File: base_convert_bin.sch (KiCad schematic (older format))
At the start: 36 parts, among them Q18 Q_PNP_BEC, Q19 Q_PNP_BEC, Q20 Q_PNP_BEC, Q21 Q_PNP_BEC, Q22 Q_NPN_BEC, Q23 Q_NPN_BEC, Q24 Q_NPN_BEC, Q25 Q_NPN_BEC

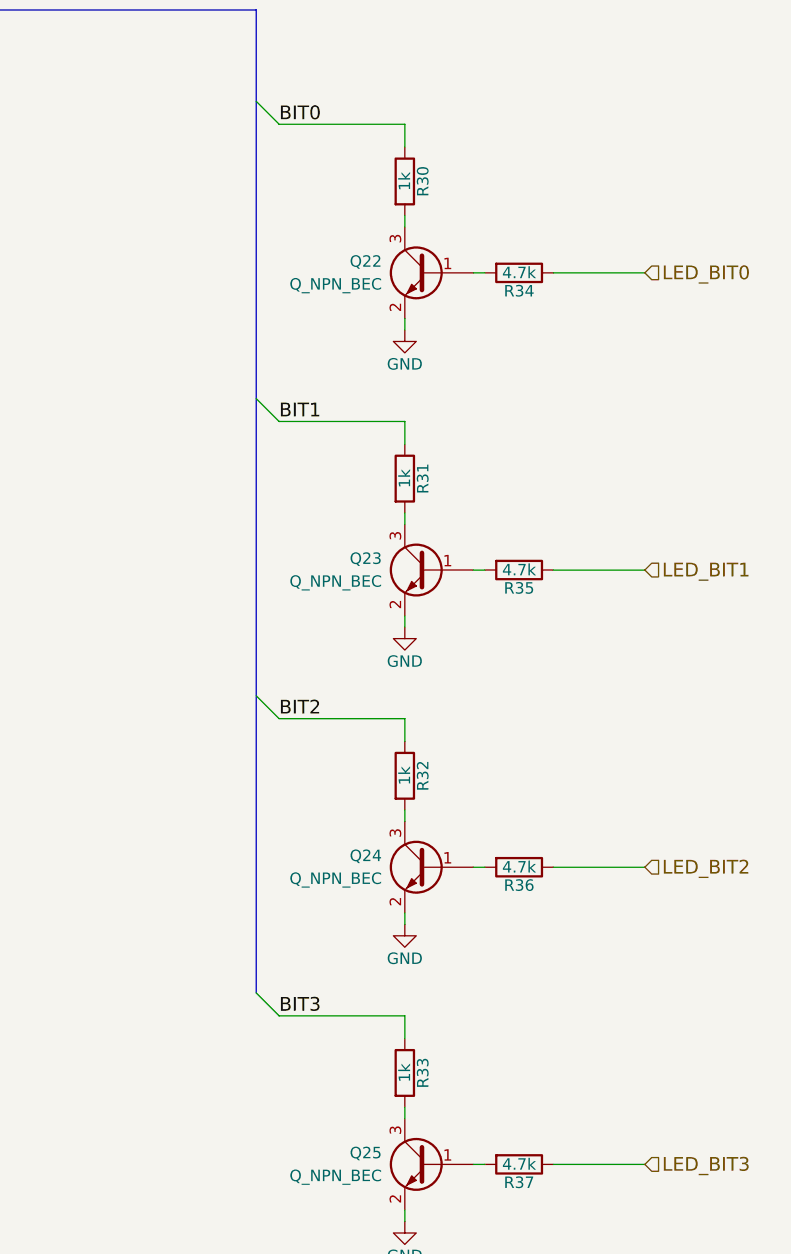
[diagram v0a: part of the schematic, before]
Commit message: change led current limit resistor value
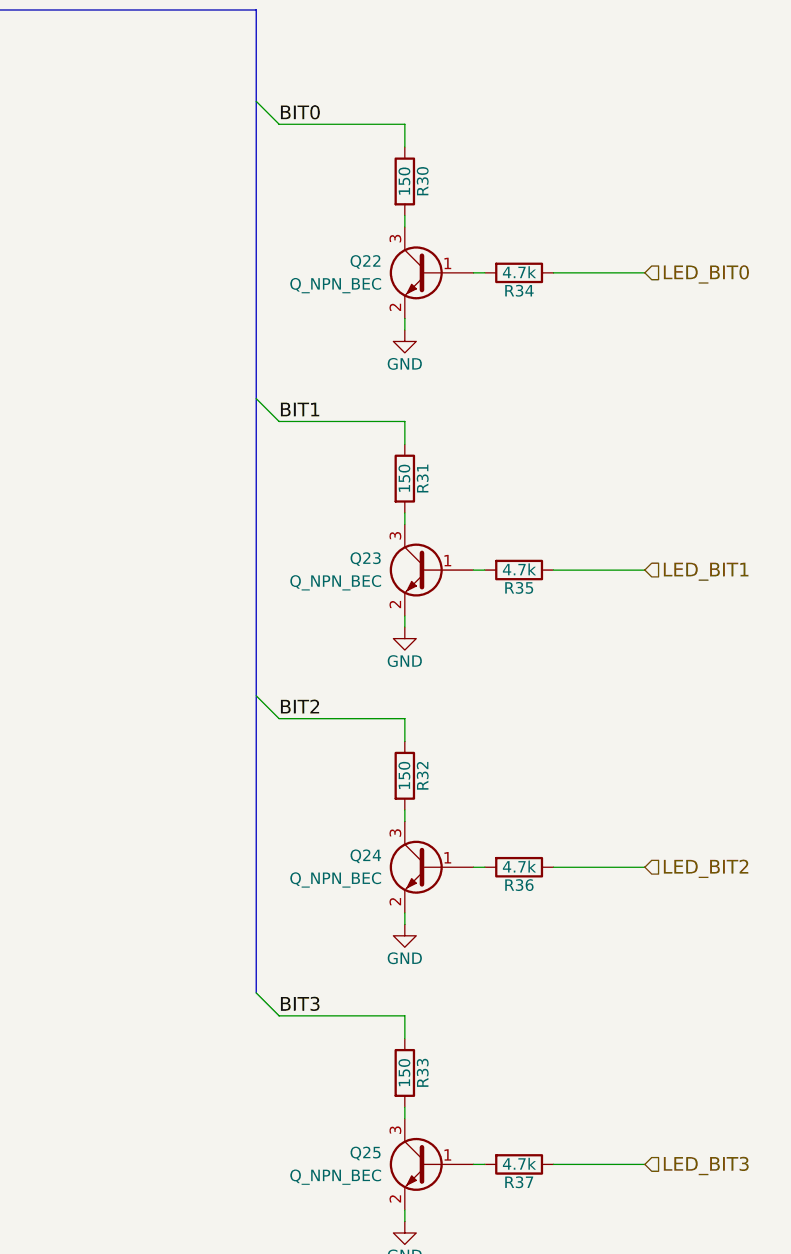
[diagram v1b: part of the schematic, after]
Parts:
- R30, R31, R32, R33: value 1k -> 150; Description (none) -> NONE; Manufacture (none) -> NONE; Mfg Part Number (none) -> NONE; Package (none) -> NONE
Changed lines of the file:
@@
 P 8250 1750
 F 0 "R30" V 8330 1750 50  0000 C CNN
-F 1 "1k" V 8250 1750 50  0000 C CNN
+F 1 "150" V 8250 1750 50  0000 C CNN
 F 2 "Resistors_SMD:R_0603" V 8180 1750 50  0001 C CNN
 F 3 "" H 8250 1750 50  0001 C CNN
+F 4 "NONE" H 8250 1750 60  0001 C CNN "Manufacture"
+F 5 "NONE" H 8250 1750 60  0001 C CNN "Mfg Part Number"
+F 6 "NONE" H 8250 1750 60  0001 C CNN "Package"
+F 7 "NONE" H 8250 1750 60  0001 C CNN "Description"
 	1    8250 1750
 	1    0    0    -1
@@
 P 8250 3050
 F 0 "R31" V 8330 3050 50  0000 C CNN
-F 1 "1k" V 8250 3050 50  0000 C CNN
+F 1 "150" V 8250 3050 50  0000 C CNN
 F 2 "Resistors_SMD:R_0603" V 8180 3050 50  0001 C CNN
 F 3 "" H 8250 3050 50  0001 C CNN
+F 4 "NONE" H 8250 3050 60  0001 C CNN "Manufacture"
+F 5 "NONE" H 8250 3050 60  0001 C CNN "Mfg Part Number"
+F 6 "NONE" H 8250 3050 60  0001 C CNN "Package"
+F 7 "NONE" H 8250 3050 60  0001 C CNN "Description"
 	1    8250 3050
 	1    0    0    -1
@@
 P 8250 4350
 F 0 "R32" V 8330 4350 50  0000 C CNN
-F 1 "1k" V 8250 4350 50  0000 C CNN
+F 1 "150" V 8250 4350 50  0000 C CNN
 F 2 "Resistors_SMD:R_0603" V 8180 4350 50  0001 C CNN
 F 3 "" H 8250 4350 50  0001 C CNN
+F 4 "NONE" H 8250 4350 60  0001 C CNN "Manufacture"
+F 5 "NONE" H 8250 4350 60  0001 C CNN "Mfg Part Number"
+F 6 "NONE" H 8250 4350 60  0001 C CNN "Package"
+F 7 "NONE" H 8250 4350 60  0001 C CNN "Description"
 	1    8250 4350
 	1    0    0    -1
@@
 P 8250 5650
 F 0 "R33" V 8330 5650 50  0000 C CNN
-F 1 "1k" V 8250 5650 50  0000 C CNN
+F 1 "150" V 8250 5650 50  0000 C CNN
 F 2 "Resistors_SMD:R_0603" V 8180 5650 50  0001 C CNN
 F 3 "" H 8250 5650 50  0001 C CNN
+F 4 "NONE" H 8250 5650 60  0001 C CNN "Manufacture"
+F 5 "NONE" H 8250 5650 60  0001 C CNN "Mfg Part Number"
+F 6 "NONE" H 8250 5650 60  0001 C CNN "Package"
+F 7 "NONE" H 8250 5650 60  0001 C CNN "Description"
 	1    8250 5650
 	1    0    0    -1

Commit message: update switch fields
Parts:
- R30, R31, R32, R33: Description NONE -> (none); Manufacture NONE -> (none); Mfg Part Number NONE -> (none); Package NONE -> (none)
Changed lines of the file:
@@
 F 2 "Resistors_SMD:R_0603" V 8180 1750 50  0001 C CNN
 F 3 "" H 8250 1750 50  0001 C CNN
-F 4 "NONE" H 8250 1750 60  0001 C CNN "Manufacture"
-F 5 "NONE" H 8250 1750 60  0001 C CNN "Mfg Part Number"
-F 6 "NONE" H 8250 1750 60  0001 C CNN "Package"
-F 7 "NONE" H 8250 1750 60  0001 C CNN "Description"
 	1    8250 1750
 	1    0    0    -1
@@
 $EndComp
 $Comp
-L VCC #PWR30
+L VCC #PWR29
 U 1 1 5AEDDAFD
 P 4300 750
-F 0 "#PWR30" H 4300 600 50  0001 C CNN
+F 0 "#PWR29" H 4300 600 50  0001 C CNN
 F 1 "VCC" H 4300 900 50  0000 C CNN
 F 2 "" H 4300 750 50  0001 C CNN
@@
 $EndComp
 $Comp
-L GND #PWR34
+L GND #PWR33
 U 1 1 5AEE40C6
 P 8250 2400
-F 0 "#PWR34" H 8250 2150 50  0001 C CNN
+F 0 "#PWR33" H 8250 2150 50  0001 C CNN
 F 1 "GND" H 8250 2250 50  0000 C CNN
 F 2 "" H 8250 2400 50  0001 C CNN
@@
 F 2 "Resistors_SMD:R_0603" V 8180 3050 50  0001 C CNN
 F 3 "" H 8250 3050 50  0001 C CNN
-F 4 "NONE" H 8250 3050 60  0001 C CNN "Manufacture"
-F 5 "NONE" H 8250 3050 60  0001 C CNN "Mfg Part Number"
-F 6 "NONE" H 8250 3050 60  0001 C CNN "Package"
-F 7 "NONE" H 8250 3050 60  0001 C CNN "Description"
 	1    8250 3050
 	1    0    0    -1
@@
 $EndComp
 $Comp
-L GND #PWR35
+L GND #PWR34
 U 1 1 5AEEC0D0
 P 8250 3700
-F 0 "#PWR35" H 8250 3450 50  0001 C CNN
+F 0 "#PWR34" H 8250 3450 50  0001 C CNN
 F 1 "GND" H 8250 3550 50  0000 C CNN
 F 2 "" H 8250 3700 50  0001 C CNN
@@
 F 2 "Resistors_SMD:R_0603" V 8180 4350 50  0001 C CNN
 F 3 "" H 8250 4350 50  0001 C CNN
-F 4 "NONE" H 8250 4350 60  0001 C CNN "Manufacture"
-F 5 "NONE" H 8250 4350 60  0001 C CNN "Mfg Part Number"
-F 6 "NONE" H 8250 4350 60  0001 C CNN "Package"
-F 7 "NONE" H 8250 4350 60  0001 C CNN "Description"
 	1    8250 4350
 	1    0    0    -1
@@
 $EndComp
 $Comp
-L GND #PWR36
+L GND #PWR35
 U 1 1 5AEEC4A2
 P 8250 5000
-F 0 "#PWR36" H 8250 4750 50  0001 C CNN
+F 0 "#PWR35" H 8250 4750 50  0001 C CNN
 F 1 "GND" H 8250 4850 50  0000 C CNN
 F 2 "" H 8250 5000 50  0001 C CNN
@@
 F 2 "Resistors_SMD:R_0603" V 8180 5650 50  0001 C CNN
 F 3 "" H 8250 5650 50  0001 C CNN
-F 4 "NONE" H 8250 5650 60  0001 C CNN "Manufacture"
-F 5 "NONE" H 8250 5650 60  0001 C CNN "Mfg Part Number"
-F 6 "NONE" H 8250 5650 60  0001 C CNN "Package"
-F 7 "NONE" H 8250 5650 60  0001 C CNN "Description"
 	1    8250 5650
 	1    0    0    -1
@@
 $EndComp
 $Comp
-L GND #PWR37
+L GND #PWR36
 U 1 1 5AEEC4C6
 P 8250 6300
-F 0 "#PWR37" H 8250 6050 50  0001 C CNN
+F 0 "#PWR36" H 8250 6050 50  0001 C CNN
 F 1 "GND" H 8250 6150 50  0000 C CNN
 F 2 "" H 8250 6300 50  0001 C CNN
@@
 $EndComp
 $Comp
-L VCC #PWR31
+L VCC #PWR30
 U 1 1 5AEECB34
 P 4300 2400
-F 0 "#PWR31" H 4300 2250 50  0001 C CNN
+F 0 "#PWR30" H 4300 2250 50  0001 C CNN
 F 1 "VCC" H 4300 2550 50  0000 C CNN
 F 2 "" H 4300 2400 50  0001 C CNN
@@
 $EndComp
 $Comp
-L VCC #PWR32
+L VCC #PWR31
 U 1 1 5AEED02A
 P 4300 4100
-F 0 "#PWR32" H 4300 3950 50  0001 C CNN
+F 0 "#PWR31" H 4300 3950 50  0001 C CNN
 F 1 "VCC" H 4300 4250 50  0000 C CNN
 F 2 "" H 4300 4100 50  0001 C CNN
@@
 $EndComp
 $Comp
-L VCC #PWR33
+L VCC #PWR32
 U 1 1 5AEED070
 P 4300 5750
-F 0 "#PWR33" H 4300 5600 50  0001 C CNN
+F 0 "#PWR32" H 4300 5600 50  0001 C CNN
 F 1 "VCC" H 4300 5900 50  0000 C CNN
 F 2 "" H 4300 5750 50  0001 C CNN

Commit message: update leds fields
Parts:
- D1: footprint LEDs:LED_D5.0mm -> LEDs:LED_0805; Description (none) -> LED RED CLEAR 0805 SMD; Manufacture (none) -> Wurth Electronics Inc.; Mfg Part Number (none) -> 150080RS75000; Package (none) -> 0805
- D10: footprint LEDs:LED_D5.0mm -> LEDs:LED_0805; Description (none) -> LED RED CLEAR 0805 SMD; Manufacture (none) -> Wurth Electronics Inc.; Mfg Part Number (none) -> 150080RS75001; Package (none) -> 0805
- D11: footprint LEDs:LED_D5.0mm -> LEDs:LED_0805; Description (none) -> LED RED CLEAR 0805 SMD; Manufacture (none) -> Wurth Electronics Inc.; Mfg Part Number (none) -> 150080RS75002; Package (none) -> 0805
- D12: footprint LEDs:LED_D5.0mm -> LEDs:LED_0805; Description (none) -> LED RED CLEAR 0805 SMD; Manufacture (none) -> Wurth Electronics Inc.; Mfg Part Number (none) -> 150080RS75003; Package (none) -> 0805
- D13: footprint LEDs:LED_D5.0mm -> LEDs:LED_0805; Description (none) -> LED RED CLEAR 0805 SMD; Manufacture (none) -> Wurth Electronics Inc.; Mfg Part Number (none) -> 150080RS75004; Package (none) -> 0805
- D14: footprint LEDs:LED_D5.0mm -> LEDs:LED_0805; Description (none) -> LED RED CLEAR 0805 SMD; Manufacture (none) -> Wurth Electronics Inc.; Mfg Part Number (none) -> 150080RS75005; Package (none) -> 0805
- D15: footprint LEDs:LED_D5.0mm -> LEDs:LED_0805; Description (none) -> LED RED CLEAR 0805 SMD; Manufacture (none) -> Wurth Electronics Inc.; Mfg Part Number (none) -> 150080RS75006; Package (none) -> 0805
- D16: footprint LEDs:LED_D5.0mm -> LEDs:LED_0805; Description (none) -> LED RED CLEAR 0805 SMD; Manufacture (none) -> Wurth Electronics Inc.; Mfg Part Number (none) -> 150080RS75007; Package (none) -> 0805
- D2: footprint LEDs:LED_D5.0mm -> LEDs:LED_0805; Description (none) -> LED RED CLEAR 0805 SMD; Manufacture (none) -> Wurth Electronics Inc.; Mfg Part Number (none) -> 150080RS75008; Package (none) -> 0805
- D3: footprint LEDs:LED_D5.0mm -> LEDs:LED_0805; Description (none) -> LED RED CLEAR 0805 SMD; Manufacture (none) -> Wurth Electronics Inc.; Mfg Part Number (none) -> 150080RS75009; Package (none) -> 0805
- D4: footprint LEDs:LED_D5.0mm -> LEDs:LED_0805; Description (none) -> LED RED CLEAR 0805 SMD; Manufacture (none) -> Wurth Electronics Inc.; Mfg Part Number (none) -> 150080RS75010; Package (none) -> 0805
- D5: footprint LEDs:LED_D5.0mm -> LEDs:LED_0805; Description (none) -> LED RED CLEAR 0805 SMD; Manufacture (none) -> Wurth Electronics Inc.; Mfg Part Number (none) -> 150080RS75011; Package (none) -> 0805
- D6: footprint LEDs:LED_D5.0mm -> LEDs:LED_0805; Description (none) -> LED RED CLEAR 0805 SMD; Manufacture (none) -> Wurth Electronics Inc.; Mfg Part Number (none) -> 150080RS75012; Package (none) -> 0805
- D7: footprint LEDs:LED_D5.0mm -> LEDs:LED_0805; Description (none) -> LED RED CLEAR 0805 SMD; Manufacture (none) -> Wurth Electronics Inc.; Mfg Part Number (none) -> 150080RS75013; Package (none) -> 0805
- D8: footprint LEDs:LED_D5.0mm -> LEDs:LED_0805; Description (none) -> LED RED CLEAR 0805 SMD; Manufacture (none) -> Wurth Electronics Inc.; Mfg Part Number (none) -> 150080RS75014; Package (none) -> 0805
- D9: footprint LEDs:LED_D5.0mm -> LEDs:LED_0805; Description (none) -> LED RED CLEAR 0805 SMD; Manufacture (none) -> Wurth Electronics Inc.; Mfg Part Number (none) -> 150080RS75015; Package (none) -> 0805

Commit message: add led light pipes
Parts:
- D1, D10, D11, D12, D13, D14, D15, D16, D2, D3, D4, D5, D6, D7, D8, D9: footprint LEDs:LED_0805 -> LightPipe_Bivar:LED_0805_LightPipe_VLP
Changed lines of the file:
@@
 F 0 "D13" H 5200 1650 50  0000 C CNN
 F 1 "BIT0" H 5200 1450 50  0000 C CNN
-F 2 "LEDs:LED_0805" H 5200 1550 50  0001 C CNN
+F 2 "LightPipe_Bivar:LED_0805_LightPipe_VLP" H 5200 1550 50  0001 C CNN
 F 3 "http://katalog.we-online.de/led/datasheet/150080RS75000.pdf" H 5200 1550 50  0001 C CNN
 F 4 "LED RED CLEAR 0805 SMD" H 5200 1750 50  0001 C CNN "Description"
@@
 F 0 "D9" H 4900 1650 50  0000 C CNN
 F 1 "BIT1" H 4900 1450 50  0000 C CNN
-F 2 "LEDs:LED_0805" H 4900 1550 50  0001 C CNN
+F 2 "LightPipe_Bivar:LED_0805_LightPipe_VLP" H 4900 1550 50  0001 C CNN
 F 3 "http://katalog.we-online.de/led/datasheet/150080RS75000.pdf" H 4900 1550 50  0001 C CNN
 F 4 "LED RED CLEAR 0805 SMD" H 4900 1750 50  0001 C CNN "Description"
@@
 F 0 "D5" H 4600 1650 50  0000 C CNN
 F 1 "BIT2" H 4600 1450 50  0000 C CNN
-F 2 "LEDs:LED_0805" H 4600 1550 50  0001 C CNN
+F 2 "LightPipe_Bivar:LED_0805_LightPipe_VLP" H 4600 1550 50  0001 C CNN
 F 3 "http://katalog.we-online.de/led/datasheet/150080RS75000.pdf" H 4600 1550 50  0001 C CNN
 F 4 "LED RED CLEAR 0805 SMD" H 4600 1750 50  0001 C CNN "Description"
@@
 F 0 "D1" H 4300 1650 50  0000 C CNN
 F 1 "BIT3" H 4300 1450 50  0000 C CNN
-F 2 "LEDs:LED_0805" H 4300 1550 50  0001 C CNN
+F 2 "LightPipe_Bivar:LED_0805_LightPipe_VLP" H 4300 1550 50  0001 C CNN
 F 3 "http://katalog.we-online.de/led/datasheet/150080RS75000.pdf" H 4300 1550 50  0001 C CNN
 F 4 "Wurth Electronics Inc." H 4300 1750 50  0001 C CNN "Manufacture"
@@
 F 0 "D14" H 5200 3300 50  0000 C CNN
 F 1 "BIT4" H 5200 3100 50  0000 C CNN
-F 2 "LEDs:LED_0805" H 5200 3200 50  0001 C CNN
+F 2 "LightPipe_Bivar:LED_0805_LightPipe_VLP" H 5200 3200 50  0001 C CNN
 F 3 "http://katalog.we-online.de/led/datasheet/150080RS75000.pdf" H 5200 3200 50  0001 C CNN
 F 4 "LED RED CLEAR 0805 SMD" H 5200 3400 50  0001 C CNN "Description"
@@
 F 0 "D10" H 4900 3300 50  0000 C CNN
 F 1 "BIT5" H 4900 3100 50  0000 C CNN
-F 2 "LEDs:LED_0805" H 4900 3200 50  0001 C CNN
+F 2 "LightPipe_Bivar:LED_0805_LightPipe_VLP" H 4900 3200 50  0001 C CNN
 F 3 "http://katalog.we-online.de/led/datasheet/150080RS75000.pdf" H 4900 3200 50  0001 C CNN
 F 4 "LED RED CLEAR 0805 SMD" H 4900 3400 50  0001 C CNN "Description"
@@
 F 0 "D6" H 4600 3300 50  0000 C CNN
 F 1 "BIT6" H 4600 3100 50  0000 C CNN
-F 2 "LEDs:LED_0805" H 4600 3200 50  0001 C CNN
+F 2 "LightPipe_Bivar:LED_0805_LightPipe_VLP" H 4600 3200 50  0001 C CNN
 F 3 "http://katalog.we-online.de/led/datasheet/150080RS75000.pdf" H 4600 3200 50  0001 C CNN
 F 4 "LED RED CLEAR 0805 SMD" H 4600 3400 50  0001 C CNN "Description"
@@
 F 0 "D2" H 4300 3300 50  0000 C CNN
 F 1 "BIT7" H 4300 3100 50  0000 C CNN
-F 2 "LEDs:LED_0805" H 4300 3200 50  0001 C CNN
+F 2 "LightPipe_Bivar:LED_0805_LightPipe_VLP" H 4300 3200 50  0001 C CNN
 F 3 "http://katalog.we-online.de/led/datasheet/150080RS75000.pdf" H 4300 3200 50  0001 C CNN
 F 4 "LED RED CLEAR 0805 SMD" H 4300 3400 50  0001 C CNN "Description"
@@
 F 0 "D15" H 5200 5000 50  0000 C CNN
 F 1 "BIT8" H 5200 4800 50  0000 C CNN
-F 2 "LEDs:LED_0805" H 5200 4900 50  0001 C CNN
+F 2 "LightPipe_Bivar:LED_0805_LightPipe_VLP" H 5200 4900 50  0001 C CNN
 F 3 "http://katalog.we-online.de/led/datasheet/150080RS75000.pdf" H 5200 4900 50  0001 C CNN
 F 4 "LED RED CLEAR 0805 SMD" H 5200 5100 50  0001 C CNN "Description"
@@
 F 0 "D11" H 4900 5000 50  0000 C CNN
 F 1 "BIT9" H 4900 4800 50  0000 C CNN
-F 2 "LEDs:LED_0805" H 4900 4900 50  0001 C CNN
+F 2 "LightPipe_Bivar:LED_0805_LightPipe_VLP" H 4900 4900 50  0001 C CNN
 F 3 "http://katalog.we-online.de/led/datasheet/150080RS75000.pdf" H 4900 4900 50  0001 C CNN
 F 4 "LED RED CLEAR 0805 SMD" H 4900 5100 50  0001 C CNN "Description"
@@
 F 0 "D7" H 4600 5000 50  0000 C CNN
 F 1 "BIT10" H 4600 4800 50  0000 C CNN
-F 2 "LEDs:LED_0805" H 4600 4900 50  0001 C CNN
+F 2 "LightPipe_Bivar:LED_0805_LightPipe_VLP" H 4600 4900 50  0001 C CNN
 F 3 "http://katalog.we-online.de/led/datasheet/150080RS75000.pdf" H 4600 4900 50  0001 C CNN
 F 4 "LED RED CLEAR 0805 SMD" H 4600 5100 50  0001 C CNN "Description"
@@
 F 0 "D3" H 4300 5000 50  0000 C CNN
 F 1 "BIT11" H 4300 4800 50  0000 C CNN
-F 2 "LEDs:LED_0805" H 4300 4900 50  0001 C CNN
+F 2 "LightPipe_Bivar:LED_0805_LightPipe_VLP" H 4300 4900 50  0001 C CNN
 F 3 "http://katalog.we-online.de/led/datasheet/150080RS75000.pdf" H 4300 4900 50  0001 C CNN
 F 4 "LED RED CLEAR 0805 SMD" H 4300 5100 50  0001 C CNN "Description"
@@
 F 0 "D16" H 5200 6650 50  0000 C CNN
 F 1 "BIT12" H 5200 6450 50  0000 C CNN
-F 2 "LEDs:LED_0805" H 5200 6550 50  0001 C CNN
+F 2 "LightPipe_Bivar:LED_0805_LightPipe_VLP" H 5200 6550 50  0001 C CNN
 F 3 "http://katalog.we-online.de/led/datasheet/150080RS75000.pdf" H 5200 6550 50  0001 C CNN
 F 4 "LED RED CLEAR 0805 SMD" H 5200 6750 50  0001 C CNN "Description"
@@
 F 0 "D12" H 4900 6650 50  0000 C CNN
 F 1 "BIT13" H 4900 6450 50  0000 C CNN
-F 2 "LEDs:LED_0805" H 4900 6550 50  0001 C CNN
+F 2 "LightPipe_Bivar:LED_0805_LightPipe_VLP" H 4900 6550 50  0001 C CNN
 F 3 "http://katalog.we-online.de/led/datasheet/150080RS75000.pdf" H 4900 6550 50  0001 C CNN
 F 4 "LED RED CLEAR 0805 SMD" H 4900 6750 50  0001 C CNN "Description"
@@
 F 0 "D8" H 4600 6650 50  0000 C CNN
 F 1 "BIT14" H 4600 6450 50  0000 C CNN
-F 2 "LEDs:LED_0805" H 4600 6550 50  0001 C CNN
+F 2 "LightPipe_Bivar:LED_0805_LightPipe_VLP" H 4600 6550 50  0001 C CNN
 F 3 "http://katalog.we-online.de/led/datasheet/150080RS75000.pdf" H 4600 6550 50  0001 C CNN
 F 4 "LED RED CLEAR 0805 SMD" H 4600 6750 50  0001 C CNN "Description"
@@
 F 0 "D4" H 4300 6650 50  0000 C CNN
 F 1 "BIT15" H 4300 6450 50  0000 C CNN
-F 2 "LEDs:LED_0805" H 4300 6550 50  0001 C CNN
+F 2 "LightPipe_Bivar:LED_0805_LightPipe_VLP" H 4300 6550 50  0001 C CNN
 F 3 "http://katalog.we-online.de/led/datasheet/150080RS75000.pdf" H 4300 6550 50  0001 C CNN
 F 4 "LED RED CLEAR 0805 SMD" H 4300 6750 50  0001 C CNN "Description"
